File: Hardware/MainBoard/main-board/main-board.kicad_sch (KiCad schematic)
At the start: 0 parts

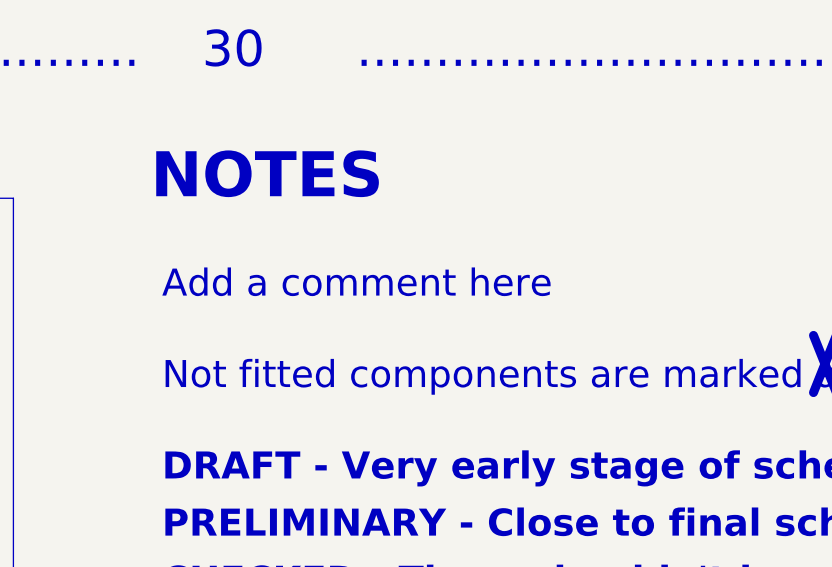
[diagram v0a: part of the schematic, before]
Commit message: add details, need to change TC amp gain for different voltage and temperature
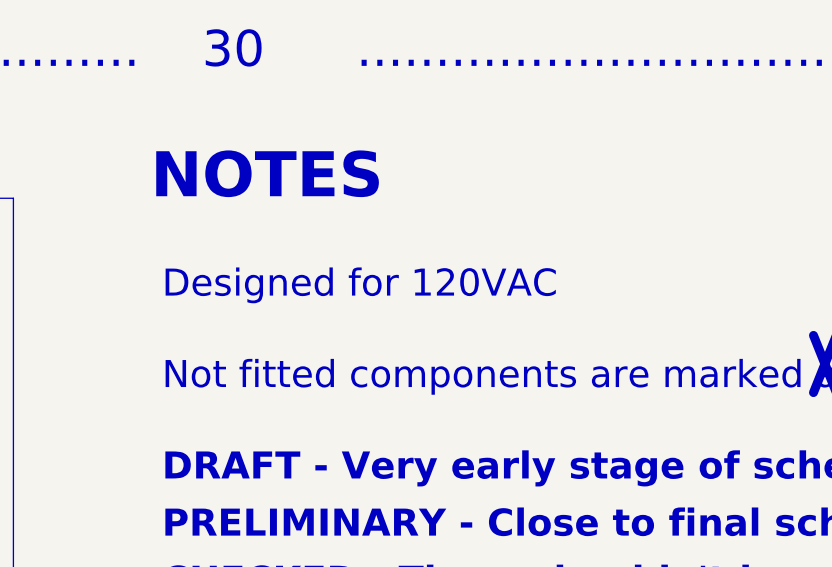
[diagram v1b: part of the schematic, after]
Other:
- note added: "Designed for 120VAC"
- note removed: "Add a comment here"
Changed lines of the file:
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@@
 		)
 	)
-	(text "Add a comment here"
+	(text "Designed for 120VAC"
 		(exclude_from_sim no)
 		(at 222.25 177.8 0)
